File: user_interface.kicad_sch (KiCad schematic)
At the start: 33 parts, among them J3 Внутр. коннектор потенциометр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, J4 Внутр. коннектор галлетника (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, SW1 Кнопка тактовая 6x6 без фикса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, SW2 Кнопка тактовая 6x6 без фикса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, SW3 Кнопка тактовая 6x6 без фикса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, SW4 Кнопка тактовая 6x6 без фикса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, SW5 Кнопка тактовая 6x6 без фикса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, SW6 Кнопка тактовая 6x6 без фикса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

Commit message: all unit test pass
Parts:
- C22, C23, C24, C32: value 100nF -> 100n
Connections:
- net LED_AC_A: now also LED5.2 (A); no longer LED5.1 (K)
- net LED_AC_DRV: now also LED5.1 (K); no longer LED5.2 (A)
- net LED_DEFROST_GLASS_A: now also LED1.2 (A); no longer LED1.1 (K)
- net LED_DEFROST_GLASS_DRV: now also LED1.1 (K); no longer LED1.2 (A)
- net LED_DRY_GLASS_A: now also LED4.2 (A); no longer LED4.1 (K)
- net LED_DRY_GLASS_DRV: now also LED4.1 (K); no longer LED4.2 (A)
- net LED_FACE_A: now also LED2.2 (A); no longer LED2.1 (K)
- net LED_FACE_DRV: now also LED2.1 (K); no longer LED2.2 (A)
- net LED_FEET_A: now also LED3.2 (A); no longer LED3.1 (K)
- net LED_FEET_DRV: now also LED3.1 (K); no longer LED3.2 (A)
- net LED_RECIRC_A: now also LED6.2 (A); no longer LED6.1 (K)
- net LED_RECIRC_DRV: now also LED6.1 (K); no longer LED6.2 (A)

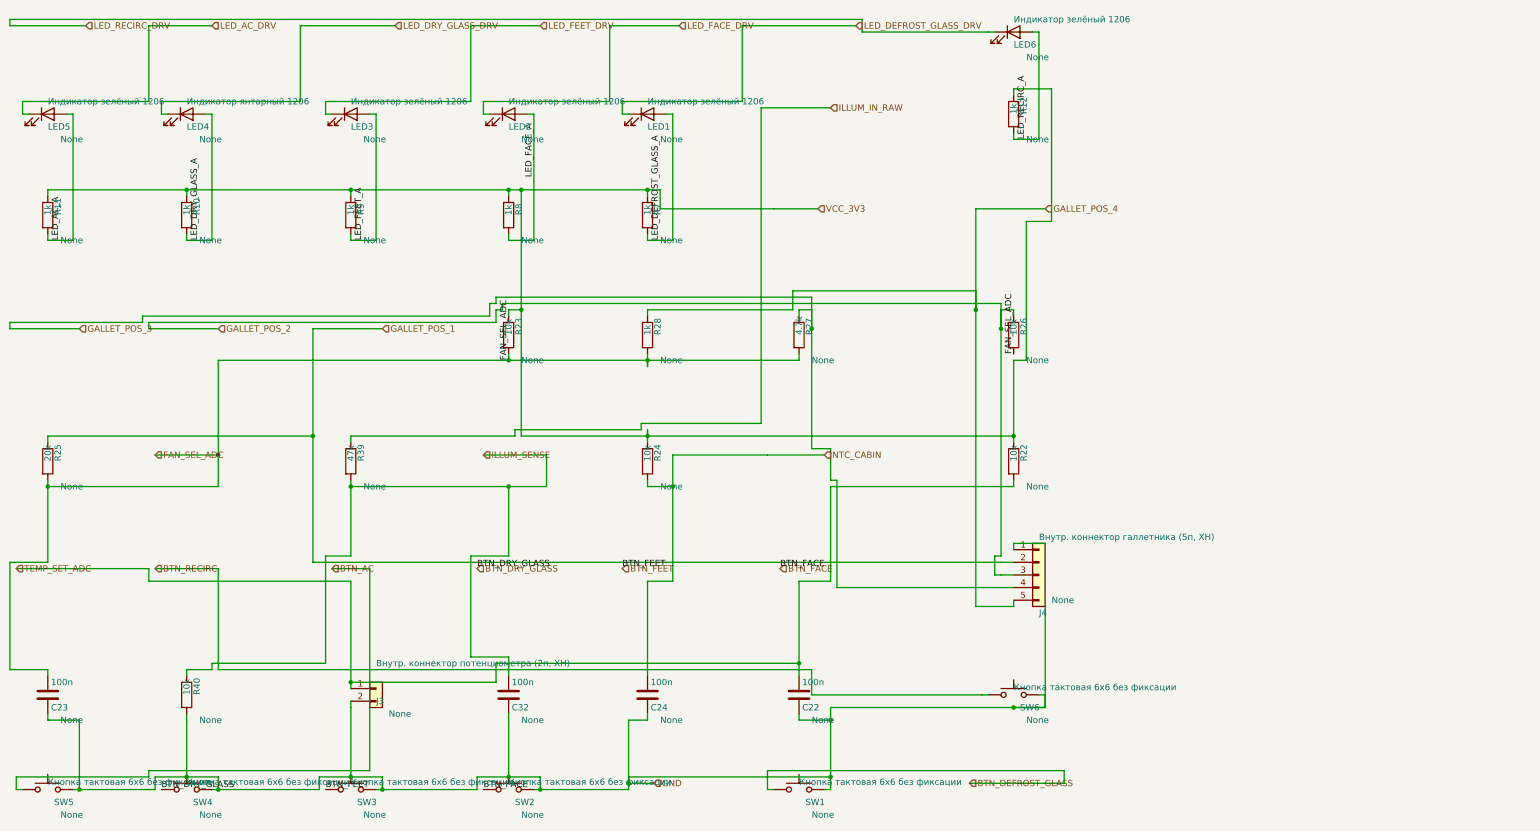
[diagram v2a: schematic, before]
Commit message: optimazed load to kicad
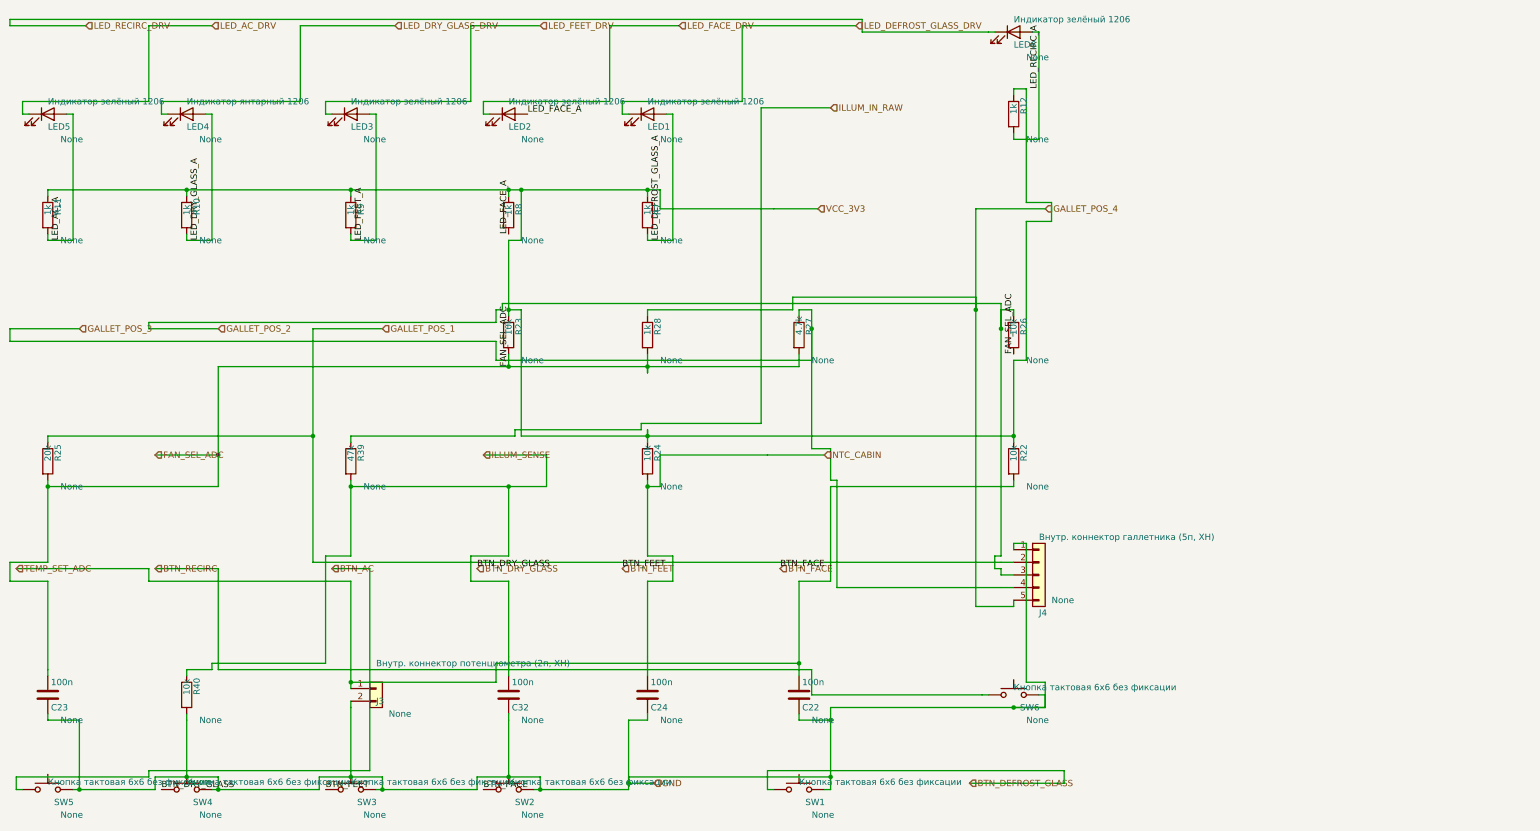
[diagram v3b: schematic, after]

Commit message: tests_fix
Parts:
- C22, C23, C24, C32, J3, J4, LED1, LED2, LED3, LED4, LED5, LED6, R10, R11, R12, R22, R23, R24, R25, R26, R27, R28, R39, R40, R7, R8, R9, SW1, SW2, SW3, SW4, SW5, SW6: hierarchy_path (none) -> /c5a034c1-1f54-4e7e-8711-0930d2b4314e/01b6ae8b-8809-4f95-98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
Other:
- title: (none) -> climate_control_niva_travel

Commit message: refactoring
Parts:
- C22, C23, C24, C32, J3, J4, LED1, LED2, LED3, LED4, LED5, LED6, R10, R11, R12, R22, R23, R24, R25, R26, R27, R28, R39, R40, R7, R8, R9, SW1, SW2, SW3, SW4, SW5, SW6: hierarchy_path /c5a034c1-1f54-4e7e-8711-0930d2b4314e/01b6ae8b-8809-4f95-98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 -> (none)
